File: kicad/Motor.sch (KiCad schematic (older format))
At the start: 5 parts, among them P1 Motor_L, P2 Motor_R, U2 DRV8835

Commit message: 部品を配置
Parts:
- C2, C3: footprint Capacitors_SMD:C_0201 -> Capacitors_SMD:C_0201_NoSilk
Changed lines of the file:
@@
 $Descr A4 11693 8268
 encoding utf-8
-Sheet 2 15
+Sheet 2 16
 Title ""
 Date ""
@@
 F 0 "C3" H 4025 3750 50  0000 L CNN
 F 1 "0.1u" H 4025 3550 50  0000 L CNN
-F 2 "Capacitors_SMD:C_0201" H 4038 3500 50  0001 C CNN
+F 2 "Capacitors_SMD:C_0201_NoSilk" H 4038 3500 50  0001 C CNN
 F 3 "" H 4000 3650 50  0000 C CNN
 	1    4000 3650
@@
 F 0 "C2" H 3725 3750 50  0000 L CNN
 F 1 "0.1u" H 3725 3550 50  0000 L CNN
-F 2 "Capacitors_SMD:C_0201" H 3738 3500 50  0001 C CNN
+F 2 "Capacitors_SMD:C_0201_NoSilk" H 3738 3500 50  0001 C CNN
 F 3 "" H 3700 3650 50  0000 C CNN
 	1    3700 3650

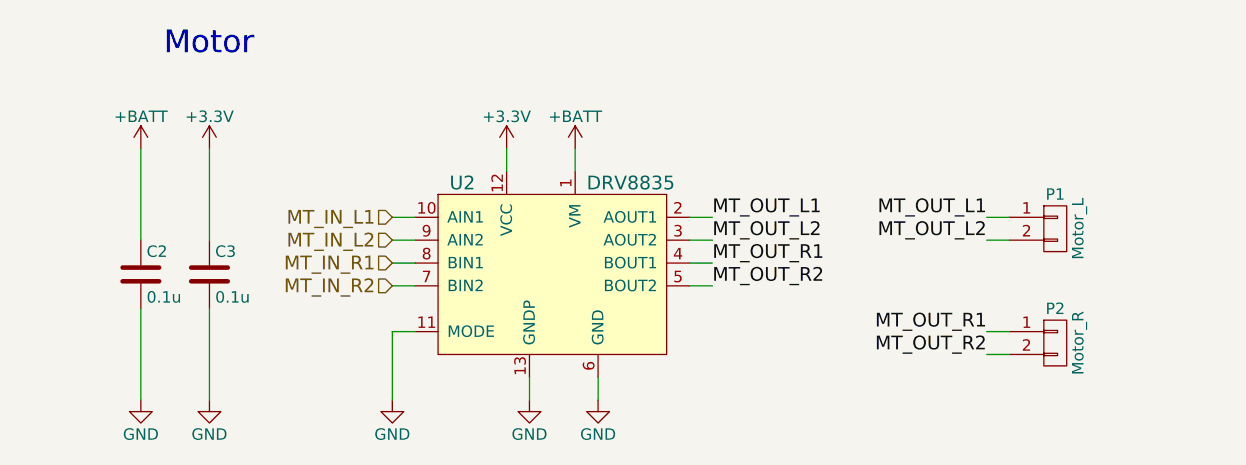
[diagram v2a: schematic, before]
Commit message: 回路を編集 ToFを除去
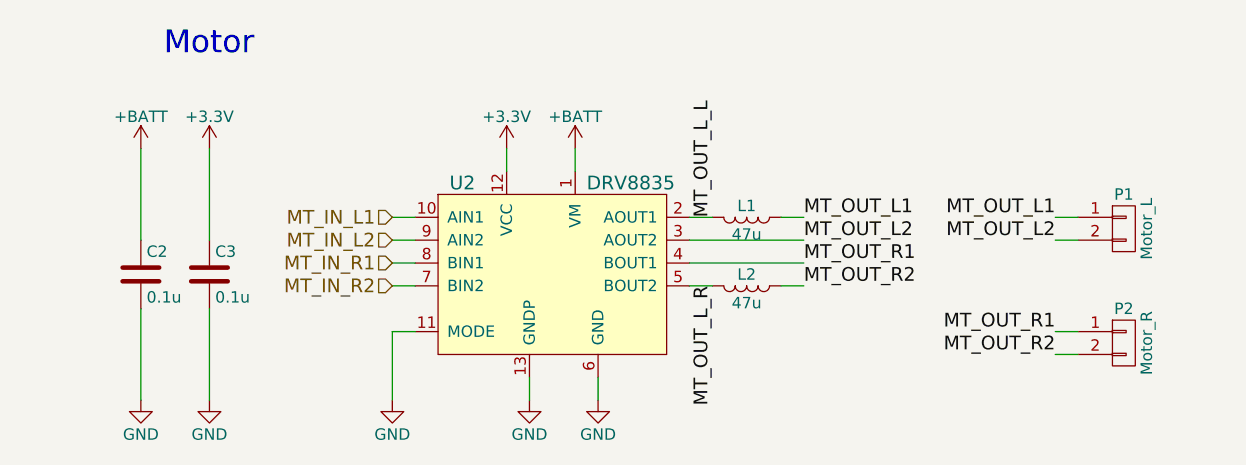
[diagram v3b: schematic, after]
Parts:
- added L1, L2: 47u, mouse:L_4018, symbol L
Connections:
- net MT_OUT_L1: now also L1.1; no longer U2.2 (AOUT1)
- net MT_OUT_R2: now also L2.1; no longer U2.5 (BOUT2)
- new net MT_OUT_L_L: L1.2, U2.2 (AOUT1)
- new net MT_OUT_L_R: L2.2, U2.5 (BOUT2)
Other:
- moved on the sheet: P1, P2
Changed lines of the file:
@@
 $Descr A4 11693 8268
 encoding utf-8
-Sheet 2 16
+Sheet 2 15
 Title ""
 Date ""
@@
 	1    0    0    -1
 $EndComp
-Wire Wire Line
-	5300 3100 5300 3200
-Wire Wire Line
-	5600 3100 5600 3200
 $Comp
 L GND #PWR07
@@
 	1    0    0    -1
 $EndComp
-Wire Wire Line
-	5400 4200 5400 4100
 $Comp
 L GND #PWR08
@@
 	1    0    0    -1
 $EndComp
-Wire Wire Line
-	5700 4200 5700 4100
 $Comp
 L GND #PWR09
@@
 	1    0    0    -1
 $EndComp
-Wire Wire Line
-	4800 4200 4800 3900
-Wire Wire Line
-	4800 3900 4900 3900
-Text Label 6200 3400 0    60   ~ 0
+Text Label 6600 3400 0    60   ~ 0
 MT_OUT_L1
-Text Label 6200 3500 0    60   ~ 0
+Text Label 6600 3500 0    60   ~ 0
 MT_OUT_L2
 Text HLabel 4800 3400 0    60   Input ~ 0
@@
 	1    0    0    -1
 $EndComp
-Wire Wire Line
-	4000 3500 4000 3100
-Wire Wire Line
-	4000 3800 4000 4200
 $Comp
 L +BATT #PWR011
@@
 	1    0    0    -1
 $EndComp
-Text Label 6200 3600 0    60   ~ 0
+Text Label 6600 3600 0    60   ~ 0
 MT_OUT_R1
-Text Label 6200 3700 0    60   ~ 0
+Text Label 6600 3700 0    60   ~ 0
 MT_OUT_R2
-Wire Wire Line
-	6200 3400 6100 3400
-Wire Wire Line
-	6100 3500 6200 3500
-Wire Wire Line
-	6200 3600 6100 3600
-Wire Wire Line
-	6100 3700 6200 3700
 Text HLabel 4800 3600 0    60   Input ~ 0
 MT_IN_R1
 Text HLabel 4800 3700 0    60   Input ~ 0
 MT_IN_R2
-Wire Wire Line
-	4800 3400 4900 3400
-Wire Wire Line
-	4900 3500 4800 3500
-Wire Wire Line
-	4800 3600 4900 3600
-Wire Wire Line
-	4900 3700 4800 3700
 $Comp
 L CONN_01X02 P1
 U 1 1 589D679E
-P 7700 3450
-F 0 "P1" H 7700 3600 50  0000 C CNN
-F 1 "Motor_L" V 7800 3450 50  0000 C CNN
-F 2 "mouse:SMD_conn_2" H 7700 3450 50  0001 C CNN
-F 3 "" H 7700 3450 50  0000 C CNN
-	1    7700 3450
+P 8000 3450
+F 0 "P1" H 8000 3600 50  0000 C CNN
+F 1 "Motor_L" V 8100 3450 50  0000 C CNN
+F 2 "mouse:SMD_conn_2" H 8000 3450 50  0001 C CNN
+F 3 "" H 8000 3450 50  0000 C CNN
+	1    8000 3450
 	1    0    0    -1
 $EndComp
@@
 L CONN_01X02 P2
 U 1 1 589D680E
-P 7700 3950
-F 0 "P2" H 7700 4100 50  0000 C CNN
-F 1 "Motor_R" V 7800 3950 50  0000 C CNN
-F 2 "mouse:SMD_conn_2" H 7700 3950 50  0001 C CNN
-F 3 "" H 7700 3950 50  0000 C CNN
-	1    7700 3950
-	1    0    0    -1
-$EndComp
-Text Label 7400 3400 2    60   ~ 0
+P 8000 3950
+F 0 "P2" H 8000 4100 50  0000 C CNN
+F 1 "Motor_R" V 8100 3950 50  0000 C CNN
+F 2 "mouse:SMD_conn_2" H 8000 3950 50  0001 C CNN
+F 3 "" H 8000 3950 50  0000 C CNN
+	1    8000 3950
+	1    0    0    -1
+$EndComp
+Text Label 7700 3400 2    60   ~ 0
 MT_OUT_L1
-Text Label 7400 3500 2    60   ~ 0
+Text Label 7700 3500 2    60   ~ 0
 MT_OUT_L2
-Text Label 7400 3900 2    60   ~ 0
+Text Label 7700 3900 2    60   ~ 0
 MT_OUT_R1
-Text Label 7400 4000 2    60   ~ 0
+Text Label 7700 4000 2    60   ~ 0
 MT_OUT_R2
-Wire Wire Line
-	7400 4000 7500 4000
-Wire Wire Line
-	7500 3900 7400 3900
-Wire Wire Line
-	7400 3400 7500 3400
-Wire Wire Line
-	7500 3500 7400 3500
 $Comp
 L +3.3V #PWR012
@@
 	1    0    0    -1
 $EndComp
+$Comp
+L L L1
+U 1 1 5B66FC72
+P 6350 3400
+F 0 "L1" V 6300 3400 50  0000 C CNN
+F 1 "47u" V 6425 3400 50  0000 C CNN
+F 2 "mouse:L_4018" H 6350 3400 50  0001 C CNN
+F 3 "" H 6350 3400 50  0001 C CNN
+	1    6350 3400
+	0    1    1    0
+$EndComp
+$Comp
+L L L2
+U 1 1 5B66FD2C
+P 6350 3700
+F 0 "L2" V 6300 3700 50  0000 C CNN
+F 1 "47u" V 6425 3700 50  0000 C CNN
+F 2 "mouse:L_4018" H 6350 3700 50  0001 C CNN
+F 3 "" H 6350 3700 50  0001 C CNN
+	1    6350 3700
+	0    1    1    0
+$EndComp
+Wire Wire Line
+	5300 3100 5300 3200
+Wire Wire Line
+	5600 3100 5600 3200
+Wire Wire Line
+	5400 4200 5400 4100
+Wire Wire Line
+	5700 4200 5700 4100
+Wire Wire Line
+	4800 4200 4800 3900
+Wire Wire Line
+	4800 3900 4900 3900
+Wire Wire Line
+	4000 3500 4000 3100
+Wire Wire Line
+	4000 3800 4000 4200
+Wire Wire Line
+	6200 3400 6100 3400
+Wire Wire Line
+	6100 3500 6600 3500
+Wire Wire Line
+	6100 3600 6600 3600
+Wire Wire Line
+	6100 3700 6200 3700
+Wire Wire Line
+	4800 3400 4900 3400
+Wire Wire Line
+	4900 3500 4800 3500
+Wire Wire Line
+	4800 3600 4900 3600
+Wire Wire Line
+	4900 3700 4800 3700
+Wire Wire Line
+	7700 4000 7800 4000
+Wire Wire Line
+	7800 3900 7700 3900
+Wire Wire Line
+	7700 3400 7800 3400
+Wire Wire Line
+	7800 3500 7700 3500
 Wire Wire Line
 	3700 4200 3700 3800
 Wire Wire Line
 	3700 3500 3700 3100
+Wire Wire Line
+	6600 3400 6500 3400
+Wire Wire Line
+	6500 3700 6600 3700
+Text Label 6200 3400 1    60   ~ 0
+MT_OUT_L_L
+Text Label 6200 3700 3    60   ~ 0
+MT_OUT_L_R
 $EndSCHEMATC

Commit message: 部品を配置 kicad5
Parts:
- removed P1: Motor_L, mouse:SMD_conn_2, symbol CONN_01X02
- removed P2: Motor_R, mouse:SMD_conn_2, symbol CONN_01X02
- added J1: Motor_L, mouse:SMD_conn_2, symbol Connector_Generic:Conn_01x02
- added J2: Motor_R, mouse:SMD_conn_2, symbol Connector_Generic:Conn_01x02
- C2, C3: symbol C -> Device:C
- L1, L2: symbol L -> Device:L
- U2: symbol DRV8835 -> KERISE:DRV8835
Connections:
- net MT_OUT_L1: now also J1.1 (Pin_1)
- net MT_OUT_L2: now also J1.2 (Pin_2)
- net MT_OUT_L_R: now also U2.4 (BOUT1); no longer U2.5 (BOUT2)
- net MT_OUT_R1: now also L2.1, J2.1 (Pin_1); no longer U2.4 (BOUT1)
- net MT_OUT_R2: now also U2.5 (BOUT2), J2.2 (Pin_2); no longer L2.1
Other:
- moved on the sheet: L2
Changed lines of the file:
@@
-EESchema Schematic File Version 2
-LIBS:power
-LIBS:device
-LIBS:transistors
-LIBS:conn
-LIBS:linear
-LIBS:regul
-LIBS:74xx
-LIBS:cmos4000
-LIBS:adc-dac
-LIBS:memory
-LIBS:xilinx
-LIBS:microcontrollers
-LIBS:dsp
-LIBS:microchip
-LIBS:analog_switches
-LIBS:motorola
-LIBS:texas
-LIBS:intel
-LIBS:audio
-LIBS:interface
-LIBS:digital-audio
-LIBS:philips
-LIBS:display
-LIBS:cypress
-LIBS:siliconi
-LIBS:opto
-LIBS:atmel
-LIBS:contrib
-LIBS:valves
-LIBS:KERISE
-LIBS:74xgxx
-LIBS:ac-dc
-LIBS:actel
-LIBS:allegro
-LIBS:Altera
-LIBS:analog_devices
-LIBS:battery_management
-LIBS:bbd
-LIBS:bosch
-LIBS:brooktre
-LIBS:cmos_ieee
-LIBS:dc-dc
-LIBS:diode
-LIBS:elec-unifil
-LIBS:ESD_Protection
-LIBS:ftdi
-LIBS:gennum
-LIBS:hc11
-LIBS:ir
-LIBS:Lattice
-LIBS:leds
-LIBS:maxim
-LIBS:mechanical
-LIBS:microchip_dspic33dsc
-LIBS:microchip_pic10mcu
-LIBS:microchip_pic12mcu
-LIBS:microchip_pic16mcu
-LIBS:microchip_pic18mcu
-LIBS:microchip_pic24mcu
-LIBS:microchip_pic32mcu
-LIBS:modules
-LIBS:motor_drivers
-LIBS:motors
-LIBS:msp430
-LIBS:nordicsemi
-LIBS:nxp
-LIBS:nxp_armmcu
-LIBS:onsemi
-LIBS:Oscillators
-LIBS:Power_Management
-LIBS:powerint
-LIBS:pspice
-LIBS:references
-LIBS:relays
-LIBS:rfcom
-LIBS:sensors
-LIBS:silabs
-LIBS:stm8
-LIBS:stm32
-LIBS:supertex
-LIBS:switches
-LIBS:transf
-LIBS:triac_thyristor
-LIBS:ttl_ieee
-LIBS:video
-LIBS:wiznet
-LIBS:Worldsemi
-LIBS:Xicor
-LIBS:zetex
-LIBS:Zilog
-LIBS:graphic_symbols
-LIBS:infineon
-LIBS:intersil
-LIBS:LEM
-LIBS:logic_programmable
-LIBS:RFSolutions
+EESchema Schematic File Version 4
 LIBS:KERISE-cache
-EELAYER 25 0
+EELAYER 26 0
 EELAYER END
 $Descr A4 11693 8268
 encoding utf-8
-Sheet 2 15
+Sheet 2 14
 Title ""
 Date ""
@@
 $EndDescr
 $Comp
-L DRV8835 U2
+L KERISE:DRV8835 U2
 U 1 1 57CA1E0F
 P 5500 3600
@@
 $EndComp
 $Comp
-L GND #PWR07
-U 1 1 57CA1E38
-P 5400 4200
-F 0 "#PWR07" H 5400 3950 50  0001 C CNN
-F 1 "GND" H 5400 4050 50  0000 C CNN
-F 2 "" H 5400 4200 50  0000 C CNN
-F 3 "" H 5400 4200 50  0000 C CNN
-	1    5400 4200
-	1    0    0    -1
-$EndComp
-$Comp
-L GND #PWR08
-U 1 1 57CA1E3F
-P 5700 4200
-F 0 "#PWR08" H 5700 3950 50  0001 C CNN
-F 1 "GND" H 5700 4050 50  0000 C CNN
-F 2 "" H 5700 4200 50  0000 C CNN
-F 3 "" H 5700 4200 50  0000 C CNN
-	1    5700 4200
-	1    0    0    -1
-$EndComp
-$Comp
-L GND #PWR09
+L power:GND #PWR011
 U 1 1 57CA1E46
 P 4800 4200
-F 0 "#PWR09" H 4800 3950 50  0001 C CNN
+F 0 "#PWR011" H 4800 3950 50  0001 C CNN
 F 1 "GND" H 4800 4050 50  0000 C CNN
 F 2 "" H 4800 4200 50  0000 C CNN
@@
 Motor
 $Comp
-L C C3
+L Device:C C3
 U 1 1 57CCEFE0
 P 4000 3650
@@
 $EndComp
 $Comp
-L GND #PWR010
-U 1 1 57CCF046
-P 4000 4200
-F 0 "#PWR010" H 4000 3950 50  0001 C CNN
-F 1 "GND" H 4000 4050 50  0000 C CNN
-F 2 "" H 4000 4200 50  0000 C CNN
-F 3 "" H 4000 4200 50  0000 C CNN
-	1    4000 4200
-	1    0    0    -1
-$EndComp
-$Comp
-L +BATT #PWR011
+L power:+BATT #PWR014
 U 1 1 57CD5BEE
 P 5600 3100
-F 0 "#PWR011" H 5600 2950 50  0001 C CNN
+F 0 "#PWR014" H 5600 2950 50  0001 C CNN
 F 1 "+BATT" H 5600 3240 50  0000 C CNN
 F 2 "" H 5600 3100 50  0000 C CNN
@@
 Text HLabel 4800 3700 0    60   Input ~ 0
 MT_IN_R2
-$Comp
-L CONN_01X02 P1
-U 1 1 589D679E
-P 8000 3450
-F 0 "P1" H 8000 3600 50  0000 C CNN
-F 1 "Motor_L" V 8100 3450 50  0000 C CNN
-F 2 "mouse:SMD_conn_2" H 8000 3450 50  0001 C CNN
-F 3 "" H 8000 3450 50  0000 C CNN
-	1    8000 3450
-	1    0    0    -1
-$EndComp
-$Comp
-L CONN_01X02 P2
-U 1 1 589D680E
-P 8000 3950
-F 0 "P2" H 8000 4100 50  0000 C CNN
-F 1 "Motor_R" V 8100 3950 50  0000 C CNN
-F 2 "mouse:SMD_conn_2" H 8000 3950 50  0001 C CNN
-F 3 "" H 8000 3950 50  0000 C CNN
-	1    8000 3950
-	1    0    0    -1
-$EndComp
 Text Label 7700 3400 2    60   ~ 0
 MT_OUT_L1
@@
 MT_OUT_R2
 $Comp
-L +3.3V #PWR012
+L power:+3.3V #PWR012
 U 1 1 589CC6A5
 P 5300 3100
@@
 $EndComp
 $Comp
-L +3.3V #PWR013
+L power:+3.3V #PWR09
 U 1 1 589CC6C6
 P 4000 3100
-F 0 "#PWR013" H 4000 2950 50  0001 C CNN
+F 0 "#PWR09" H 4000 2950 50  0001 C CNN
 F 1 "+3.3V" H 4000 3240 50  0000 C CNN
 F 2 "" H 4000 3100 50  0000 C CNN
@@
 $EndComp
 $Comp
-L +BATT #PWR014
+L power:+BATT #PWR07
 U 1 1 594721DF
 P 3700 3100
-F 0 "#PWR014" H 3700 2950 50  0001 C CNN
+F 0 "#PWR07" H 3700 2950 50  0001 C CNN
 F 1 "+BATT" H 3700 3240 50  0000 C CNN
 F 2 "" H 3700 3100 50  0000 C CNN
@@
 $EndComp
 $Comp
-L C C2
+L Device:C C2
 U 1 1 594721FA
 P 3700 3650
@@
 $EndComp
 $Comp
-L GND #PWR015
-U 1 1 59472221
-P 3700 4200
-F 0 "#PWR015" H 3700 3950 50  0001 C CNN
-F 1 "GND" H 3700 4050 50  0000 C CNN
-F 2 "" H 3700 4200 50  0000 C CNN
-F 3 "" H 3700 4200 50  0000 C CNN
-	1    3700 4200
-	1    0    0    -1
-$EndComp
-$Comp
-L L L1
+L Device:L L1
 U 1 1 5B66FC72
 P 6350 3400
@@
 $EndComp
 $Comp
-L L L2
+L Device:L L2
 U 1 1 5B66FD2C
-P 6350 3700
-F 0 "L2" V 6300 3700 50  0000 C CNN
-F 1 "47u" V 6425 3700 50  0000 C CNN
-F 2 "mouse:L_4018" H 6350 3700 50  0001 C CNN
-F 3 "" H 6350 3700 50  0001 C CNN
-	1    6350 3700
+P 6350 3600
+F 0 "L2" V 6300 3600 50  0000 C CNN
+F 1 "47u" V 6425 3600 50  0000 C CNN
+F 2 "mouse:L_4018" H 6350 3600 50  0001 C CNN
+F 3 "" H 6350 3600 50  0001 C CNN
+	1    6350 3600
 	0    1    1    0
 $EndComp
@@
 	6100 3500 6600 3500
 Wire Wire Line
-	6100 3600 6600 3600
-Wire Wire Line
-	6100 3700 6200 3700
-Wire Wire Line
 	4800 3400 4900 3400
 Wire Wire Line
@@
 Wire Wire Line
 	6600 3400 6500 3400
-Wire Wire Line
-	6500 3700 6600 3700
 Text Label 6200 3400 1    60   ~ 0
 MT_OUT_L_L
-Text Label 6200 3700 3    60   ~ 0
+Text Label 6200 3600 3    60   ~ 0
 MT_OUT_L_R
+$Comp
+L Connector_Generic:Conn_01x02 J1
+U 1 1 5B6F504A
+P 8000 3400
+F 0 "J1" H 8079 3392 50  0000 L CNN
+F 1 "Motor_L" H 8079 3301 50  0000 L CNN
+F 2 "mouse:SMD_conn_2" H 8000 3400 50  0001 C CNN
+F 3 "~" H 8000 3400 50  0001 C CNN
+	1    8000 3400
+	1    0    0    -1
+$EndComp
+$Comp
+L Connector_Generic:Conn_01x02 J2
+U 1 1 5B6F50A6
+P 8000 3900
+F 0 "J2" H 8080 3892 50  0000 L CNN
+F 1 "Motor_R" H 8080 3801 50  0000 L CNN
+F 2 "mouse:SMD_conn_2" H 8000 3900 50  0001 C CNN
+F 3 "~" H 8000 3900 50  0001 C CNN
+	1    8000 3900
+	1    0    0    -1
+$EndComp
+$Comp
+L power:GND #PWR015
+U 1 1 5B6FD311
+P 5700 4200
+F 0 "#PWR015" H 5700 3950 50  0001 C CNN
+F 1 "GND" H 5700 4050 50  0000 C CNN
+F 2 "" H 5700 4200 50  0000 C CNN
+F 3 "" H 5700 4200 50  0000 C CNN
+	1    5700 4200
+	1    0    0    -1
+$EndComp
+$Comp
+L power:GND #PWR010
+U 1 1 5B6FD364
+P 4000 4200
+F 0 "#PWR010" H 4000 3950 50  0001 C CNN
+F 1 "GND" H 4000 4050 50  0000 C CNN
+F 2 "" H 4000 4200 50  0000 C CNN
+F 3 "" H 4000 4200 50  0000 C CNN
+	1    4000 4200
+	1    0    0    -1
+$EndComp
+$Comp
+L power:GND #PWR08
+U 1 1 5B7097B0
+P 3700 4200
+F 0 "#PWR08" H 3700 3950 50  0001 C CNN
+F 1 "GND" H 3700 4050 50  0000 C CNN
+F 2 "" H 3700 4200 50  0000 C CNN
+F 3 "" H 3700 4200 50  0000 C CNN
+	1    3700 4200
+	1    0    0    -1
+$EndComp
+$Comp
+L power:GND #PWR013
+U 1 1 5B7097C9
+P 5400 4200
+F 0 "#PWR013" H 5400 3950 50  0001 C CNN
+F 1 "GND" H 5400 4050 50  0000 C CNN
+F 2 "" H 5400 4200 50  0000 C CNN
+F 3 "" H 5400 4200 50  0000 C CNN
+	1    5400 4200
+	1    0    0    -1
+$EndComp
+Wire Wire Line
+	6200 3600 6100 3600
+Wire Wire Line
+	6100 3700 6600 3700
+Wire Wire Line
+	6500 3600 6600 3600
 $EndSCHEMATC

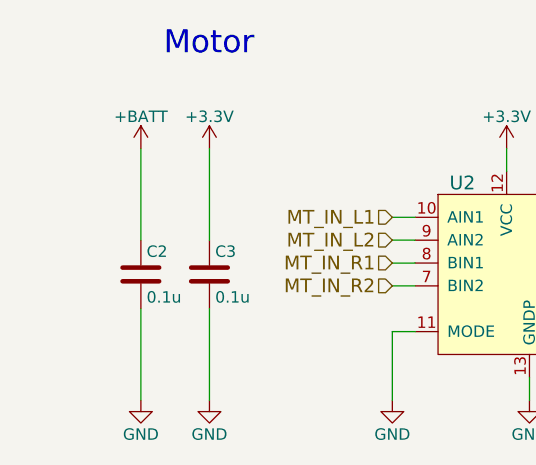
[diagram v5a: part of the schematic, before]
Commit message: フットプリントを割り当て
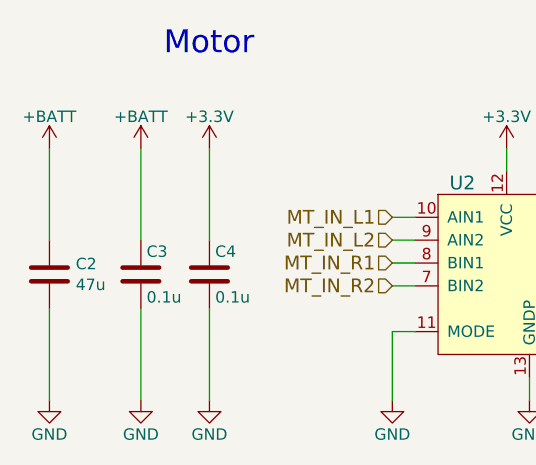
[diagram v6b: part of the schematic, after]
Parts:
- added C2: 47u, Capacitor_SMD:C_0805_2012Metric, symbol Device:C
- C3: renamed from C2; footprint Capacitors_SMD:C_0201_NoSilk -> Capacitor_SMD:C_0201_0603Metric
- C4: renamed from C3; footprint Capacitors_SMD:C_0201_NoSilk -> Capacitor_SMD:C_0201_0603Metric
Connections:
- net +BATT: now also C2.1
- net GND: now also C2.2
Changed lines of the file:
@@
 $EndComp
 $Comp
-L power:GND #PWR011
+L power:GND #PWR013
 U 1 1 57CA1E46
 P 4800 4200
-F 0 "#PWR011" H 4800 3950 50  0001 C CNN
+F 0 "#PWR013" H 4800 3950 50  0001 C CNN
 F 1 "GND" H 4800 4050 50  0000 C CNN
 F 2 "" H 4800 4200 50  0000 C CNN
@@
 Motor
 $Comp
-L Device:C C3
+L Device:C C4
 U 1 1 57CCEFE0
 P 4000 3650
-F 0 "C3" H 4025 3750 50  0000 L CNN
+F 0 "C4" H 4025 3750 50  0000 L CNN
 F 1 "0.1u" H 4025 3550 50  0000 L CNN
-F 2 "Capacitors_SMD:C_0201_NoSilk" H 4038 3500 50  0001 C CNN
+F 2 "Capacitor_SMD:C_0201_0603Metric" H 4038 3500 50  0001 C CNN
 F 3 "" H 4000 3650 50  0000 C CNN
 	1    4000 3650
@@
 $EndComp
 $Comp
-L power:+BATT #PWR014
+L power:+BATT #PWR016
 U 1 1 57CD5BEE
 P 5600 3100
-F 0 "#PWR014" H 5600 2950 50  0001 C CNN
+F 0 "#PWR016" H 5600 2950 50  0001 C CNN
 F 1 "+BATT" H 5600 3240 50  0000 C CNN
 F 2 "" H 5600 3100 50  0000 C CNN
@@
 MT_OUT_R2
 $Comp
-L power:+3.3V #PWR012
+L power:+3.3V #PWR014
 U 1 1 589CC6A5
 P 5300 3100
-F 0 "#PWR012" H 5300 2950 50  0001 C CNN
+F 0 "#PWR014" H 5300 2950 50  0001 C CNN
 F 1 "+3.3V" H 5300 3240 50  0000 C CNN
 F 2 "" H 5300 3100 50  0000 C CNN
@@
 $EndComp
 $Comp
-L power:+3.3V #PWR09
+L power:+3.3V #PWR011
 U 1 1 589CC6C6
 P 4000 3100
-F 0 "#PWR09" H 4000 2950 50  0001 C CNN
+F 0 "#PWR011" H 4000 2950 50  0001 C CNN
 F 1 "+3.3V" H 4000 3240 50  0000 C CNN
 F 2 "" H 4000 3100 50  0000 C CNN
@@
 $EndComp
 $Comp
-L power:+BATT #PWR07
+L power:+BATT #PWR09
 U 1 1 594721DF
 P 3700 3100
-F 0 "#PWR07" H 3700 2950 50  0001 C CNN
+F 0 "#PWR09" H 3700 2950 50  0001 C CNN
 F 1 "+BATT" H 3700 3240 50  0000 C CNN
 F 2 "" H 3700 3100 50  0000 C CNN
@@
 $EndComp
 $Comp
-L Device:C C2
+L Device:C C3
 U 1 1 594721FA
 P 3700 3650
-F 0 "C2" H 3725 3750 50  0000 L CNN
+F 0 "C3" H 3725 3750 50  0000 L CNN
 F 1 "0.1u" H 3725 3550 50  0000 L CNN
-F 2 "Capacitors_SMD:C_0201_NoSilk" H 3738 3500 50  0001 C CNN
+F 2 "Capacitor_SMD:C_0201_0603Metric" H 3738 3500 50  0001 C CNN
 F 3 "" H 3700 3650 50  0000 C CNN
 	1    3700 3650
@@
 $EndComp
 $Comp
-L power:GND #PWR015
+L power:GND #PWR017
 U 1 1 5B6FD311
 P 5700 4200
-F 0 "#PWR015" H 5700 3950 50  0001 C CNN
+F 0 "#PWR017" H 5700 3950 50  0001 C CNN
 F 1 "GND" H 5700 4050 50  0000 C CNN
 F 2 "" H 5700 4200 50  0000 C CNN
@@
 $EndComp
 $Comp
-L power:GND #PWR010
+L power:GND #PWR012
 U 1 1 5B6FD364
 P 4000 4200
-F 0 "#PWR010" H 4000 3950 50  0001 C CNN
+F 0 "#PWR012" H 4000 3950 50  0001 C CNN
 F 1 "GND" H 4000 4050 50  0000 C CNN
 F 2 "" H 4000 4200 50  0000 C CNN
@@
 $EndComp
 $Comp
-L power:GND #PWR08
+L power:GND #PWR010
 U 1 1 5B7097B0
 P 3700 4200
-F 0 "#PWR08" H 3700 3950 50  0001 C CNN
+F 0 "#PWR010" H 3700 3950 50  0001 C CNN
 F 1 "GND" H 3700 4050 50  0000 C CNN
 F 2 "" H 3700 4200 50  0000 C CNN
@@
 $EndComp
 $Comp
-L power:GND #PWR013
+L power:GND #PWR015
 U 1 1 5B7097C9
 P 5400 4200
-F 0 "#PWR013" H 5400 3950 50  0001 C CNN
+F 0 "#PWR015" H 5400 3950 50  0001 C CNN
 F 1 "GND" H 5400 4050 50  0000 C CNN
 F 2 "" H 5400 4200 50  0000 C CNN
@@
 Wire Wire Line
 	6500 3600 6600 3600
+$Comp
+L Device:C C2
+U 1 1 5C29DB96
+P 3300 3650
+F 0 "C2" H 3415 3696 50  0000 L CNN
+F 1 "47u" H 3415 3605 50  0000 L CNN
+F 2 "Capacitor_SMD:C_0805_2012Metric" H 3338 3500 50  0001 C CNN
+F 3 "~" H 3300 3650 50  0001 C CNN
+	1    3300 3650
+	1    0    0    -1
+$EndComp
+$Comp
+L power:GND #PWR08
+U 1 1 5C29DC0A
+P 3300 4200
+F 0 "#PWR08" H 3300 3950 50  0001 C CNN
+F 1 "GND" H 3300 4050 50  0000 C CNN
+F 2 "" H 3300 4200 50  0000 C CNN
+F 3 "" H 3300 4200 50  0000 C CNN
+	1    3300 4200
+	1    0    0    -1
+$EndComp
+Wire Wire Line
+	3300 4200 3300 3800
+$Comp
+L power:+BATT #PWR07
+U 1 1 5C29DEF5
+P 3300 3100
+F 0 "#PWR07" H 3300 2950 50  0001 C CNN
+F 1 "+BATT" H 3300 3240 50  0000 C CNN
+F 2 "" H 3300 3100 50  0000 C CNN
+F 3 "" H 3300 3100 50  0000 C CNN
+	1    3300 3100
+	1    0    0    -1
+$EndComp
+Wire Wire Line
+	3300 3100 3300 3500
 $EndSCHEMATC
